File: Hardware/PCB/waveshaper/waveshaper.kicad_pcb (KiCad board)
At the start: 2 copper layers, 189 x 174 mm, 54 parts, among them J1 AudioJack2_SwitchT, J10 2x7 IDC header, J11 Conn_01x03, J12 Conn_01x02, J13 EURO_PWR_2x5, J14 Conn_01x9, J15 Conn_01x9, J2 AudioJack2_SwitchT, J20 Conn_01x02, J3 AudioJack2_SwitchT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

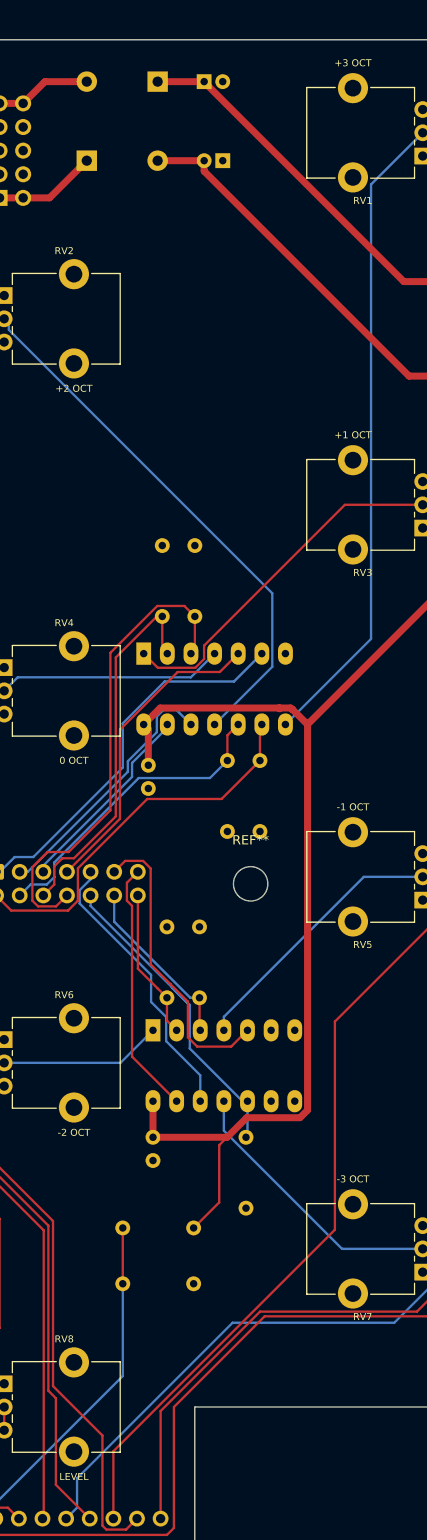
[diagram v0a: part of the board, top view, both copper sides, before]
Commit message: Directory reorg, panel work
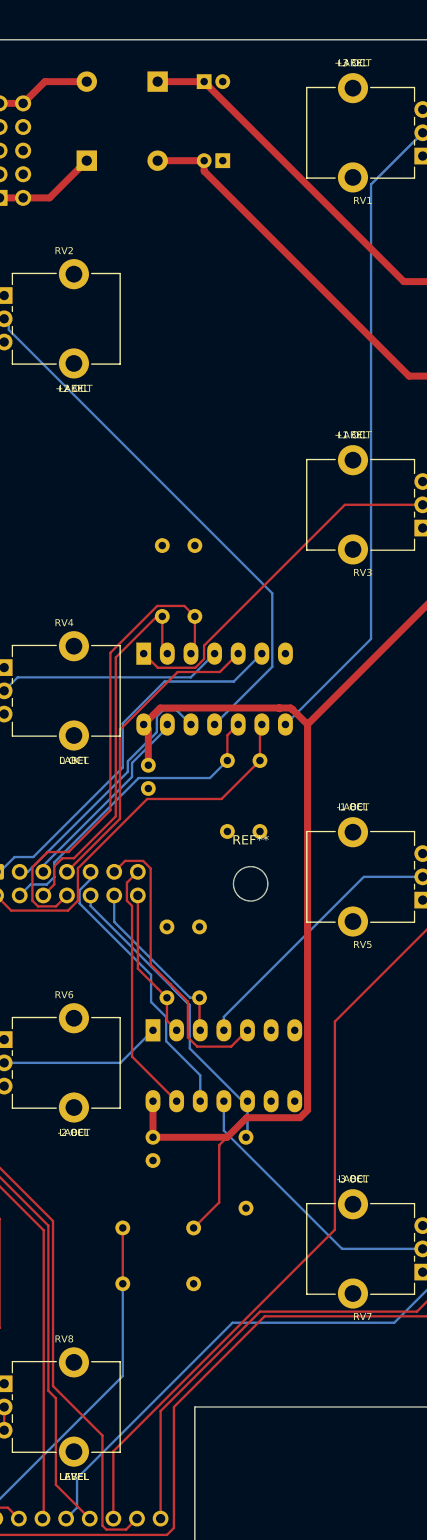
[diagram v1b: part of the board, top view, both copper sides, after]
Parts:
- added G***: LOGO, waveshaper:waveshaper-holes, F.Cu at (131.0, 106.2)
